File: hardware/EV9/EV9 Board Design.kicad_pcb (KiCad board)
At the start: 4 copper layers, 72.7 x 89.4 mm, 117 parts, among them J1 Conn_01x02_Female, J10 Conn_01x08_Female, J11 Conn_01x06_Female, J12 Conn_01x04_Female, J13 Conn_01x04_Female, J14 Conn_01x04_Female, J15 Conn_01x02_Female, J2 Conn_01x02_Female, J3 Conn_01x04_Female, J4 Conn_01x08_Male, J5 Conn_01x04_Female, J6 Conn_01x04_Female, J7 Conn_01x04_Female, J8 Conn_01x06_Female, J9 USB_C_Receptacle, SW1 SW_Push, SW2 SW_Push, SW3 SW_Push, U1 STM32F405RGTx, U11 ESP32-S3-WROOM-1-N8R2, U12 MCP73832-2-OT, U13 BM14B(0.8)-24DS-0.4V(53), U2 AMS1117-3.3, U3 CH340C, U4 USBLC6-2P6, U5 STM32F030C8Tx, U6 WM8960CGEFL/RV, Y1 Crystal_GND24

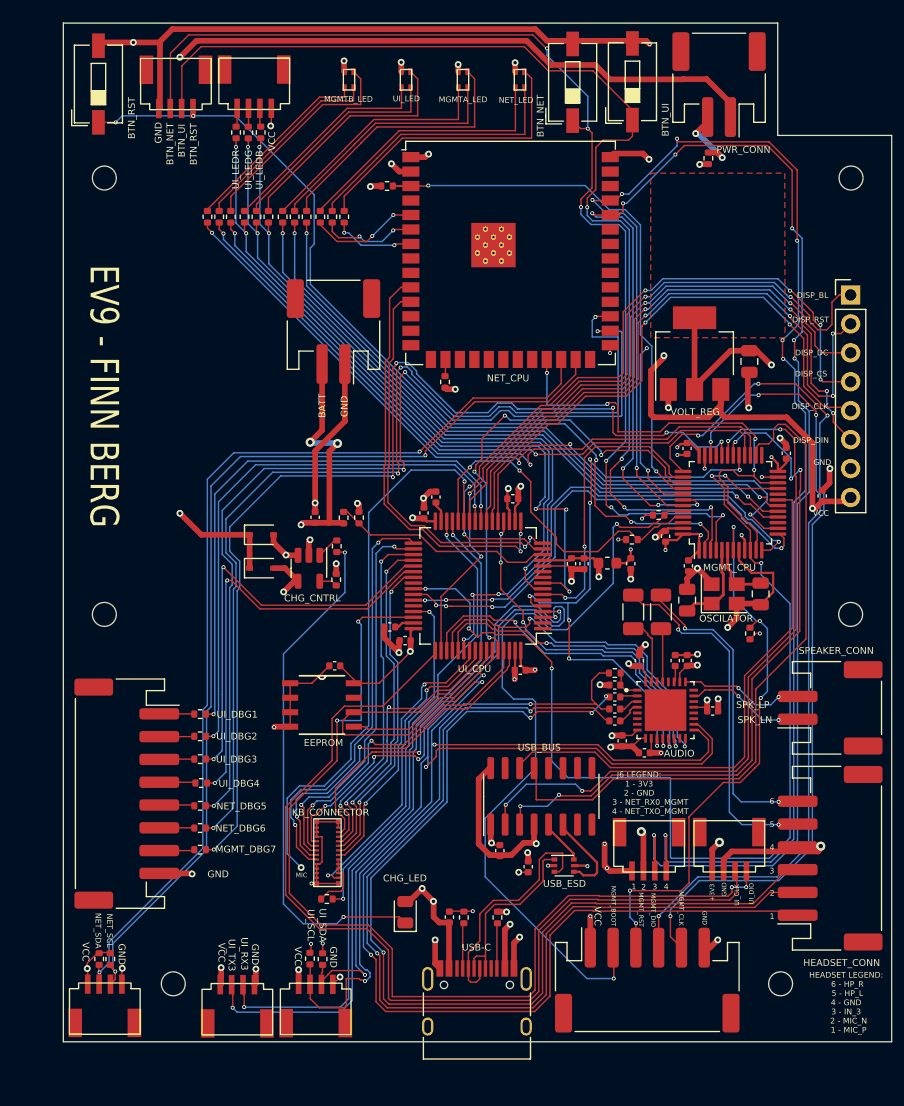
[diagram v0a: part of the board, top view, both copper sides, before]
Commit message: Removed LED, UI Serial, Net I2C connector/ changed button
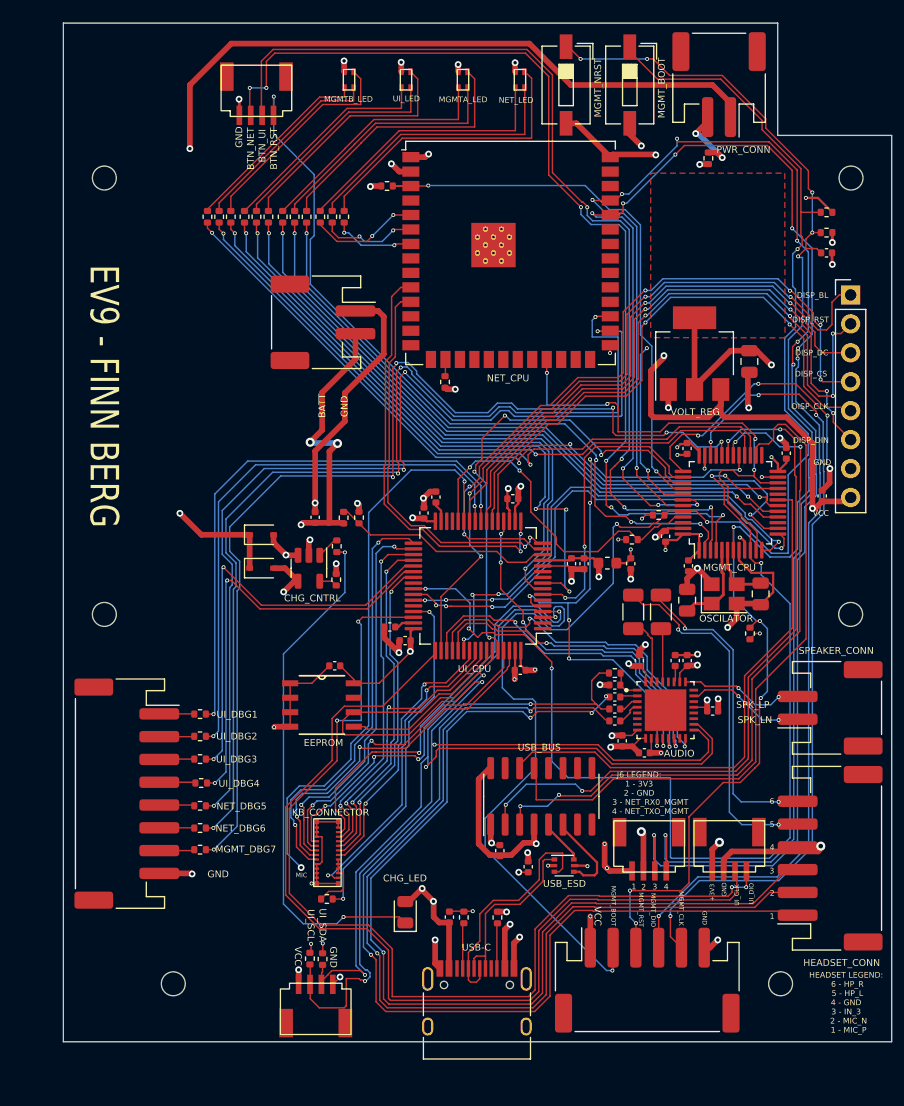
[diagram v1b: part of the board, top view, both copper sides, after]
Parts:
- removed J14, J3, J5: Conn_01x04_Female, 1x4 pin download:1x4pin 1mm connector
- removed R21: 1k5, Resistor_SMD:R_0402_1005Metric
- removed R33: 180, Resistor_SMD:R_0402_1005Metric
- removed R34, R35: 150, Resistor_SMD:R_0402_1005Metric
- removed SW1, SW2, SW3: SW_Push, Button_Switch_SMD:SW_DIP_SPSTx01_Slide_6.7x4.1mm_W6.73mm_P2.54mm_LowProfile_JPin
- added C35: 100n, Capacitor_SMD:C_0402_1005Metric, F.Cu at (181.0, 76.2)
- added R10: 4k7, Resistor_SMD:R_0402_1005Metric, F.Cu at (181.0, 72.6)
- added SW4: SW_Push, Button_Switch_SMD:SW_DIP_SPSTx01_Slide_6.7x4.1mm_W6.73mm_P2.54mm_LowProfile_JPin, F.Cu at (163.7, 61.5)
- added SW5: SW_Push, Button_Switch_SMD:SW_DIP_SPSTx01_Slide_6.7x4.1mm_W6.73mm_P2.54mm_LowProfile_JPin, F.Cu at (158.1, 61.5)
- R20: value 1k5 -> 4k7
- moved R20 90.2 mm to (181.0, 74.4), turned to 180 degrees
- moved J13 7.09 mm to (133.5, 60.7)
- moved J1 1.23 mm to (136.8, 82.3), turned to -90 degrees
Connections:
- R20 pad 2: /NET_SDA -> /MGMT_NRST
- U1 pad 29: /UI_TX3 -> unconnected-(U1-PB10-Pad29)
- U1 pad 30: /UI_RX3 -> unconnected-(U1-PB11-Pad30)
- U11 pad 24: /NET_SDA -> unconnected-(U11-IO47-Pad24)
- U11 pad 25: /NET_SCL -> unconnected-(U11-IO48-Pad25)
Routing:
- net /NET_SCL: track 86.0 -> 0.00 mm, vias 2 -> 0
- net /NET_SDA: track 85.7 -> 0.00 mm, vias 2 -> 0
- net /MGMT_NRST: track 50.2 -> 121.8 mm, vias 5 -> 10
- net GND: track 719.6 -> 649.3 mm, vias 48 -> 47
- net /MGMT_BOOT: track 68.0 -> 134.4 mm, vias 2 -> 4
- net /UI_TX3: track 60.9 -> 0.00 mm, vias 2 -> 0
- net /UI_RX3: track 59.2 -> 0.00 mm, vias 2 -> 0
- net +3.3V: track 534.8 -> 516.8 mm, vias 31 -> 30
- net /BTN_UI: track 99.9 -> 86.7 mm
- net /BTN_NET: track 100.7 -> 88.8 mm
- net /BTN_RST: track 79.7 -> 68.1 mm, vias 5 -> 4
- net /UI_LED_B: track 67.0 -> 58.2 mm, vias 5 -> 4
- net /UI_LED_R: track 62.9 -> 54.2 mm, vias 5 -> 4
- net /UI_LED_G: track 58.4 -> 49.7 mm, vias 3 -> 2
- net +BATT: track 27.2 -> 31.1 mm
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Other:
- board text added: "MGMT_NRST"
- board text removed: "NET_SCL"
- board text removed: "NET_SDA"
- board text removed: "UI_LEDB"
- board text removed: "UI_LEDG"
- board text removed: "UI_LEDR"
- board text removed: "UI_RX3"
- board text removed: "UI_TX3"
